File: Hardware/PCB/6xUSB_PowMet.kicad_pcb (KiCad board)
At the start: 2 copper layers, 73.2 x 66.8 mm, 109 parts, among them CON1 BARREL_JACK, IC1 ATMEGA32-M, P1 USB_A, P10 USB_B, P2 USB_A, P3 USB_A, P4 USB_A, P5 USB_A, P6 USB_A, P7 CONN_01X08, P8 CONN_01X03, Q1 IRFR5305PBF, U1 LM1117MP-2.5, U10 TPS5450-EP_DDA_8, U11 LTC4412, U2 LT6106, U3 LT6106, U4 LT6106, U5 LT6106, U6 LT6106, U7 LT6106, U8 AP1117E33, U9 FE1.1s, Y1 12Mhz

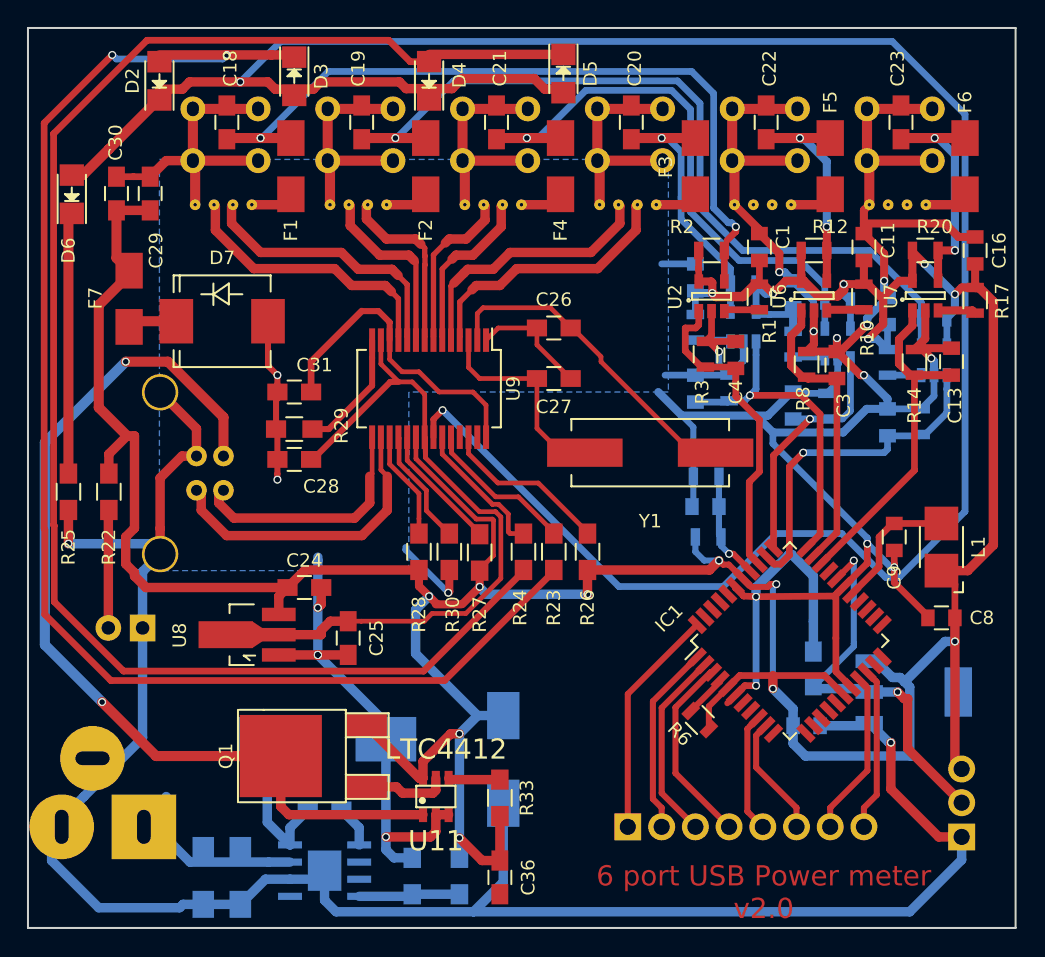
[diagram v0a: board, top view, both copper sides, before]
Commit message: Updated pcb
Updated schematic and solved some pcb mistakes
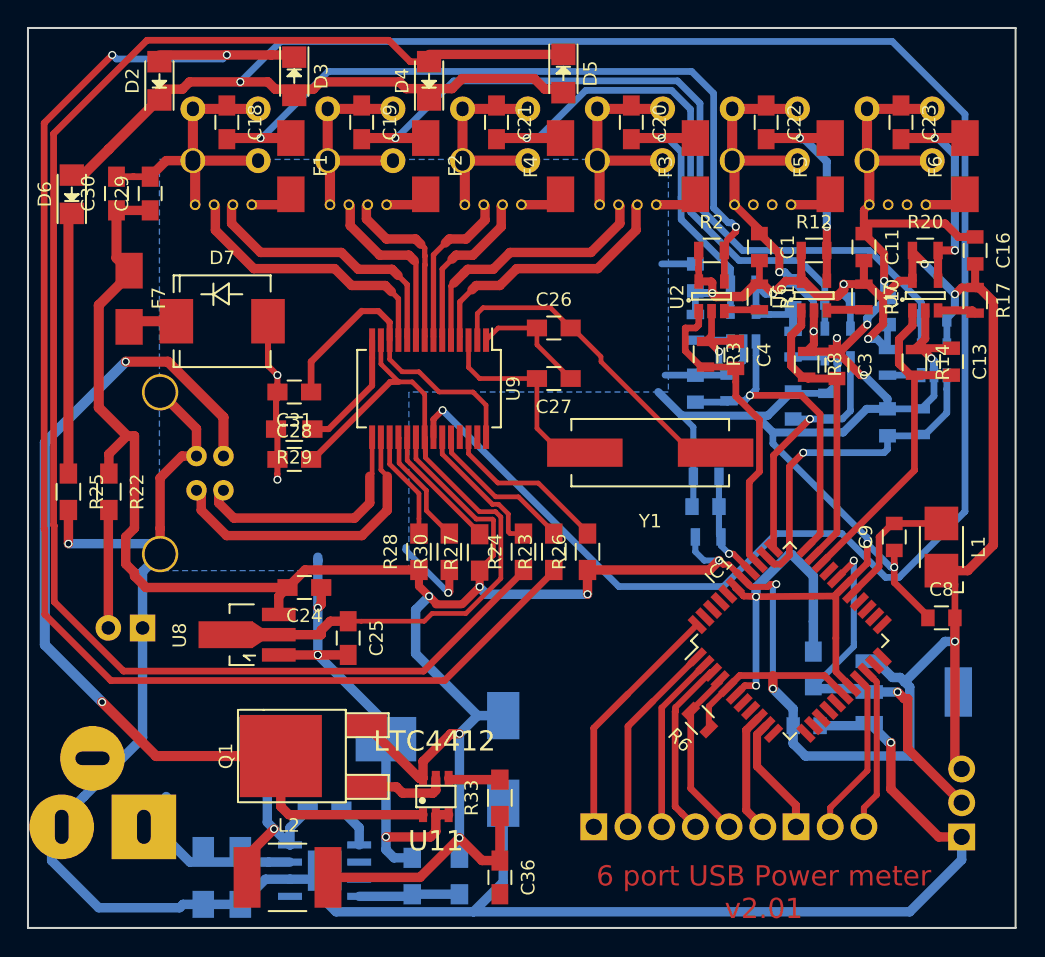
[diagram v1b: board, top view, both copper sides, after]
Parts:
- added L2: 10uH, Inductors_NEOSID:Neosid_Inductor_SM-NE56_SMD2220, F.Cu at (114.5, 111.5)
- added P9: CONN_01X03, Connect:Wafer_Vertical10x5.8x7RM2.5-3, B.Cu at (152.2, 107.8)
- P7: value CONN_01X08 -> CONN_01X06; footprint Connect:Wafer_Vertical22.5x5.8x7RM2.5-8 -> Connect:Wafer_Vertical17.5x5.8x7RM2.5-6
- moved P7 2.52 mm to (137.2, 107.8)
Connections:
- IC1 pad 4: Net-(IC1-Pad4) -> RST
- P7 pad 5: RXD -> RST
- P7 pad 6: TXD -> RXD
- R6 pad 2: Net-(IC1-Pad4) -> RST
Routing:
- net RST: track 0.00 -> 13.0 mm
- net +5V: track 305.5 -> 316.4 mm
- net Net-(C34-Pad1): track 11.7 -> 16.1 mm, vias 0 -> 1
- net Net-(IC1-Pad4): track 3.21 -> 0.00 mm
- net SS: track 17.1 -> 18.2 mm
- net MISO: track 14.4 -> 13.4 mm
- net SCK: track 14.3 -> 13.3 mm
- net GND: track 495.7 -> 494.9 mm
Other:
- board text added: "6 port USB Power meter v2.01"
- board text removed: "6 port USB Power meter v2.0"

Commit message: Upd_sch
Updated schematic and PCB
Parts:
- D7: footprint Diodes_SMD:SMC_Standard -> Diodes_SMD:SOD-123
- Y1: footprint Crystals:Crystal_HC49-SD_SMD -> Crystals:Crystal_SMD_5032_4Pads
- moved Y1 2.95 mm to (138.8, 78.7)
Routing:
- net GND: track 494.9 -> 506.6 mm, vias 21 -> 22
- net Net-(C26-Pad2): track 24.5 -> 18.7 mm
- net Net-(D7-Pad1): track 3.67 -> 5.44 mm

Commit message: Upd
Schematic updates and PCB
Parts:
- removed C32, C33: 47uF, Capacitors_SMD:C_1206_HandSoldering
- removed C34: 10n, Capacitors_SMD:C_0805_HandSoldering
- removed C35: 180uF, Capacitors_SMD:c_elec_8x10.5
- removed CON1: BARREL_JACK, Connect:JACK_ALIM
- removed L2: 10uH, Inductors_NEOSID:Neosid_Inductor_SM-NE56_SMD2220
- removed U10: TPS5450-EP_DDA_8, TPS5450-EP_DDA_8:DDA8_3X2P49
- added C37: 22uF, Capacitors_SMD:C_1206, F.Cu at (108.0, 100.2)
- added C38: 100nF, Capacitors_SMD:C_0805, F.Cu at (110.9, 103.8)
- added C39: 15nF, Capacitors_SMD:C_0805, F.Cu at (114.8, 102.5)
- added C40: 470nF, Capacitors_SMD:C_0805, F.Cu at (130.9, 101.6)
- added C41: 1uF, Capacitors_SMD:C_0805, F.Cu at (110.8, 99.8)
- added C42: 470pF, Capacitors_SMD:C_0805, F.Cu at (121.6, 112.4)
- added C43: 220uF, Capacitors_SMD:c_elec_6.3x5.3, F.Cu at (129.0, 111.2)
- added CON2: BARREL_JACK, Connect:JACK_ALIM, B.Cu at (100.8, 108.7)
- added D10: SKL14, Diodes_SMD:SOD-123, F.Cu at (108.9, 69.4)
- added D11: SK2030YD2, Diodes_SMD:DD-PAK_TO263_DualDiode, B.Cu at (139.0, 99.6)
- added D12: Power, LEDs:LED-5MM, B.Cu at (163.2, 82.0)
- added D9: Power, LEDs:LED-5MM, B.Cu at (100.2, 99.4)
- added L3: 2.2uH, Inductors:SELF-WE-PD-XXL, B.Cu at (122.8, 105.8)
- added Q2: CSD16342Q5A, Personal:AB2_SON5x6_FET, F.Cu at (114.8, 110.2)
- added Q3: CSD17577Q5A, Personal:AB2_SON5x6_FET, F.Cu at (132.4, 97.7)
- added R34: 100K, Resistors_SMD:R_0805, F.Cu at (114.1, 105.8)
- added R35: 1K07, Resistors_SMD:R_0805, F.Cu at (128.8, 104.2)
- added R36: 73K2, Capacitors_SMD:C_0805, F.Cu at (121.6, 109.4)
- added R37: 10K, Capacitors_SMD:C_0805, F.Cu at (121.6, 106.5)
- added R38: 330, Resistors_SMD:R_0805_HandSoldering, F.Cu at (104.2, 96.8)
- added U13: LM3150, Housings_SSOP:SSOP-14_5.3x6.2mm_Pitch0.65mm, F.Cu at (121.7, 101.4)
- C24: value 4.7uF -> 10uF; moved to B.Cu
- C25: value 4.7uF -> 22uF; moved to B.Cu
- C28, C36, Q1, R33, U11: moved to B.Cu
- C6: footprint Capacitors_SMD:C_0805_HandSoldering -> Capacitors_SMD:C_0805
- D2, D3, D4, D5, D6: footprint LEDs:LED_1206 -> LEDs:LED_0805
- D7: footprint Diodes_SMD:SOD-123 -> Diodes_SMD:MiniMELF_Standard
- D8: value D_Schottky -> Power; footprint Diodes_SMD:SMC_Handsoldering -> LEDs:LED-5MM
- F7: value F_Small -> 500mA
- R31: value 10K -> 330
- R32: value 3.24K -> 330
- R5: value 14K -> 15K
- U8: footprint TO_SOT_Packages_SMD:SOT89-3_Housing_Handsoldering -> TO_SOT_Packages_SMD:SOT-223; moved to B.Cu
- U9: footprint Housings_SSOP:SSOP-28_5.3x10.2mm_Pitch0.65mm -> Housings_SSOP:TSSOP-28_4.4x9.7mm_Pitch0.65mm
- moved R32 46.9 mm to (163.9, 87.2), turned to 90 degrees
- moved D8 46.7 mm to (159.9, 82.0), turned to 180 degrees
- moved R31 41.8 mm to (161.4, 87.2)
- moved U8 26.9 mm to (137.8, 88.2), turned to 0 degrees
- moved C24 26.2 mm to (140.2, 80.7), turned to 270 degrees
- moved R25 24.1 mm to (99.0, 58.9)
- moved C25 23.0 mm to (137.8, 80.5), turned to 90 degrees
- moved D1 23.0 mm to (100.2, 70.3), turned to 90 degrees
- moved C36 21.1 mm to (130.0, 90.5), turned to 0 degrees
- moved R22 17.5 mm to (108.2, 66.8), turned to 180 degrees
- moved R33 16.0 mm to (122.5, 91.5), turned to 270 degrees
- moved U11 12.1 mm to (125.7, 93.4), turned to 180 degrees
- moved C28 9.75 mm to (124.6, 82.2), turned to 90 degrees
- moved R26 8.91 mm to (131.7, 80.0), turned to 180 degrees
- moved Q1 8.85 mm to (119.0, 93.8), turned to 270 degrees
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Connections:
- net /USB hub/3V3 renamed +3.3V
- D7 pad 1: Net-(D7-Pad1) -> +5V
- D8 pad 1: Net-(C34-Pad1) -> GND
- D8 pad 2: GND -> Net-(D8-Pad2)
- F7 pad 1: +5V -> USB_P
- F7 pad 2: Net-(D7-Pad1) -> Net-(F7-Pad2)
- IC1 pad 25: Net-(IC1-Pad25) -> PC6_25
- IC1 pad 26: Net-(IC1-Pad26) -> PC7_26
- P10 pad 1: VREG -> Net-(F7-Pad2)
- Q1 pad 2: VREG -> +5V
- R22 pad 1: +5V -> USB_P
- R31 pad 1: Net-(R31-Pad1) -> PC7_26
- R31 pad 2: +5V -> Net-(D8-Pad2)
- R32 pad 1: GND -> PC6_25
- R32 pad 2: Net-(R31-Pad1) -> Net-(D12-Pad2)
- U11 pad 1: VREG -> +5V
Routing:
- net VREG: track 70.8 -> 0.00 mm, vias 2 -> 0
- net Net-(D2-Pad1): track 178.5 -> 110.1 mm
- net Net-(C42-Pad1): track 0.00 -> 59.2 mm, vias 0 -> 2
- net GND: track 506.6 -> 449.7 mm, vias 22 -> 23
- net Net-(C40-Pad1): track 0.00 -> 32.3 mm, vias 0 -> 2
- net Net-(C37-Pad1): track 0.00 -> 29.5 mm
- net Net-(C42-Pad2): track 0.00 -> 23.8 mm, vias 0 -> 2
- net +3.3V: track 53.0 -> 31.7 mm, vias 0 -> 2
- net +5V: track 316.4 -> 336.8 mm
- net Net-(D6-Pad1): track 19.4 -> 2.56 mm
- net Net-(C34-Pad1): track 16.1 -> 0.00 mm, vias 1 -> 0
- net Net-(Q2-Pad4): track 0.00 -> 15.1 mm, vias 0 -> 2
- net Net-(C32-Pad1): track 13.0 -> 0.00 mm
- net Net-(F7-Pad2): track 0.00 -> 9.16 mm
- net Net-(R26-Pad2): track 12.6 -> 4.32 mm
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- added copper zone on F.Cu, net GND
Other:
- board text added: "6 port USB Power meter v2.1"
- board text removed: "6 port USB Power meter v2.01"

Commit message: updates
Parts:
- removed D12, D8: Power, LEDs:LED-5MM
- removed D4, D5: Led_Small, LEDs:LED_0805
- removed D7: 5.1V, Diodes_SMD:MiniMELF_Standard
- removed IC1: ATMEGA32-M, Housings_QFP:TQFP-44_10x10mm_Pitch0.8mm
- removed P7: CONN_01X06, Connect:Wafer_Vertical17.5x5.8x7RM2.5-6
- removed P8, P9: CONN_01X03, Connect:Wafer_Vertical10x5.8x7RM2.5-3
- added C32: 22pF, Capacitors_SMD:C_0603, F.Cu at (146.7, 101.3)
- added C33: 0.1uF, Capacitors_SMD:C_0603, F.Cu at (149.4, 106.2)
- added C34: 100n, Capacitors_SMD:C_0805, B.Cu at (175.1, 104.0)
- added C35: 100n, Capacitors_SMD:C_0805, B.Cu at (179.5, 95.3)
- added C44: 10uF, Capacitors_SMD:C_0805, F.Cu at (185.1, 86.6)
- added C45: 10uF, Capacitors_SMD:C_0805, B.Cu at (181.9, 95.3)
- added C46: 22uF, Capacitors_Tantalum_SMD:CP_Tantalum_Case-R_EIA-2012-12_Reflow, F.Cu at (182.4, 127.0)
- added C47: 1uF, Capacitors_SMD:C_0805, F.Cu at (108.5, 124.3)
- added C48: 100n, Capacitors_SMD:C_0805, F.Cu at (202.2, 76.2)
- added C49: 1uF, Capacitors_SMD:C_0805, F.Cu at (135.6, 131.4)
- added C51: 47uF, Capacitors_SMD:C_1206, F.Cu at (200.9, 119.2)
- added C52: 18pF, Capacitors_SMD:C_0805, F.Cu at (121.8, 37.3)
- added F8: MSMF050-2, Resistors_SMD:R_1812, F.Cu at (185.8, 138.5)
- added J1: MICROUSB, kicad-libs-master:USB-MICRO-B-FCI-10118193, F.Cu at (87.2, 128.3)
- added J2: CONN_01X04, Connectors_JST:JST_EH_B04B-EH-A_04x2.50mm_Straight, F.Cu at (105.8, 140.7)
- added J3: CONN_01X11, Connectors_JST:JST_EH_B11B-EH-A_11x2.50mm_Straight, F.Cu at (139.8, 124.4)
- added L10: WE-CNSW, Inductors_SMD:L_CommonMode_Wuerth_WE-CNSW, F.Cu at (76.2, 102.5)
- added L11: WE-CBF, Inductors_SMD:L_0603, F.Cu at (120.3, 61.6)
- added L12: WE-CBF, Inductors_SMD:L_0603, F.Cu at (170.4, 45.5)
- added L2: WE-CNSW, Inductors_SMD:L_CommonMode_Wuerth_WE-CNSW, F.Cu at (135.2, 64.4)
- added L4: Bead/100MHZ/470ohm/2A, Resistors_SMD:R_0805_HandSoldering, B.Cu at (97.4, 66.0)
- added L5: WE-CNSW, Inductors_SMD:L_CommonMode_Wuerth_WE-CNSW, F.Cu at (125.7, 64.4)
- added L6: WE-CNSW, Inductors_SMD:L_CommonMode_Wuerth_WE-CNSW, F.Cu at (118.5, 64.4)
- added L7: WE-CNSW, Inductors_SMD:L_CommonMode_Wuerth_WE-CNSW, F.Cu at (109.2, 64.4)
- added L8: WE-CBF, Inductors_SMD:L_0603, F.Cu at (107.8, 61.6)
- added L9: WE-CBF, Inductors_SMD:L_0603, F.Cu at (132.8, 61.6)
- added LED1: Led_Small, Inductors_SMD:L_1806, F.Cu at (102.6, 49.7)
- added LED2: Led_Small, Inductors_SMD:L_1806, F.Cu at (115.2, 49.8)
- added LED3: Led_Small, Inductors_SMD:L_1806, F.Cu at (127.6, 49.8)
- added LED4: Led_Small, Inductors_SMD:L_1806, F.Cu at (140.1, 49.8)
- added P11: CONN_02X04, Socket_Strips:Socket_Strip_Straight_2x04, B.Cu at (162.6, 69.3)
- added P12: CONN_02X04, Socket_Strips:Socket_Strip_Straight_2x04, B.Cu at (174.4, 69.2)
- added P13: Burn, Pin_Headers:Pin_Header_Straight_2x01, B.Cu at (185.1, 78.9)
- added Q10: IRLML6401, TO_SOT_Packages_SMD:SOT-23, F.Cu at (200.4, 104.8)
- added Q5: IRLML6401, TO_SOT_Packages_SMD:SOT-23, B.Cu at (142.6, 69.8)
- added Q6: IRLML6401, TO_SOT_Packages_SMD:SOT-23, B.Cu at (158.3, 53.1)
- added Q7: IRLML6401, TO_SOT_Packages_SMD:SOT-23, F.Cu at (157.6, 65.1)
- added Q8: IRLML6401, TO_SOT_Packages_SMD:SOT-23, B.Cu at (176.6, 77.2)
- added Q9: IRLML6401, TO_SOT_Packages_SMD:SOT-23, F.Cu at (148.1, 61.8)
- added R39: 10K, Resistors_SMD:R_0805, B.Cu at (180.1, 104.0)
- added R40: 10K, Resistors_SMD:R_0805, F.Cu at (141.4, 90.8)
- added R41: 100R, Resistors_SMD:R_0805, B.Cu at (180.1, 100.1)
- added R42: 10K, Resistors_SMD:R_0805, F.Cu at (140.9, 86.8)
- added R43: 100R, Resistors_SMD:R_0805, B.Cu at (157.2, 93.2)
- added R44: 100R, Resistors_SMD:R_0805, F.Cu at (123.4, 82.8)
- added R45: 100K, Resistors_SMD:R_0805, F.Cu at (115.1, 73.0)
- added R46: 470R, Resistors_SMD:R_0805, B.Cu at (177.2, 104.0)
- added R47: 100R, Resistors_SMD:R_0805, B.Cu at (174.2, 90.8)
- added R48: 150R, Resistors_SMD:R_0805, B.Cu at (174.2, 98.0)
- added R49: 150R, Resistors_SMD:R_0805, B.Cu at (174.2, 94.3)
- added RV1: CG0603MLC-05E, Inductors_SMD:L_0603, F.Cu at (204.4, 85.4)
- added RV2: CG0603MLC-05E, Inductors_SMD:L_0603, F.Cu at (87.0, 121.2)
- added SW1: Reset, Buttons_Switches_SMD:SW_SPST_B3U-1000P, F.Cu at (179.8, 84.1)
- added SW2: Reset, Buttons_Switches_SMD:SW_SPST_B3U-3000P, F.Cu at (197.8, 130.6)
- added TP1: TEST, Measurement_Points:Measurement_Point_Round-SMD-Pad_Small, B.Cu at (169.3, 97.8)
- added U10: ESP-07v2, ESP8266:ESP-12E, F.Cu at (185.6, 105.0)
- added U12: 5v to 3.3v LDO, TO_SOT_Packages_SMD:SOT-223-3Lead_TabPin2, B.Cu at (180.2, 83.7)
- added U14: LT6106, TO_SOT_Packages_SMD:SOT-23-5, F.Cu at (147.2, 144.1)
- added Y2: 16.000 Mhz, Crystals:Crystal_SMD_5032-4pin_5.0x3.2mm, F.Cu at (147.4, 104.2)
- C1, C16, D10, R3, R8, U2, U6, U7: moved to B.Cu
- C11: value 100n -> 1nF; moved to B.Cu
- C12, C14: value 1n -> 1nF; moved to F.Cu
- C13: value 1n -> 1nF; moved to B.Cu
- C15, C17, R13, R15, U5: moved to F.Cu
- C18, C19, C20, C29: footprint Capacitors_SMD:C_0805_HandSoldering -> Capacitors_SMD:C_0805
- C2: value 1n -> 0.33uF
- C21, C22, C23: value 10uF -> 1nF; footprint Capacitors_SMD:C_0805_HandSoldering -> Capacitors_SMD:C_0805
- C24, C30: value 10uF -> 0.1uF; footprint Capacitors_SMD:C_0805_HandSoldering -> Capacitors_SMD:C_0603
- C25: value 22uF -> 22pF; footprint Capacitors_SMD:C_0805_HandSoldering -> Capacitors_SMD:C_0603
- C26: value 10pF -> 18pF; footprint Capacitors_SMD:C_0805_HandSoldering -> Capacitors_SMD:C_0805
- C27: value 10pF -> 100n; footprint Capacitors_SMD:C_0805_HandSoldering -> Capacitors_SMD:C_0805
- C28: footprint Capacitors_SMD:C_0805_HandSoldering -> Capacitors_SMD:C_0805; moved to F.Cu
- C3, C4: value 1n -> 100n; moved to B.Cu
- C31: value 10uF -> 47uF; footprint Capacitors_SMD:C_0805_HandSoldering -> Capacitors_SMD:C_1206; moved to B.Cu
- C36: value 100nF -> 10uF; footprint Capacitors_SMD:C_0805_HandSoldering -> Capacitors_SMD:C_0805
- C37: value 22uF -> 47uF
- C38: value 100nF -> 100n
- C42: value 470pF -> 1nF
- C43: value 220uF -> 330uF; footprint Capacitors_SMD:c_elec_6.3x5.3 -> Capacitors_SMD:CP_Elec_6.3x5.8; moved to B.Cu
- C6: value 10uF -> 100n
- C7: value 1n -> 100n
- D1: value Power -> USB Power; footprint LEDs:LED-5MM -> LEDs:LED_D3.0mm_Horizontal_O6.35mm_Z6.0mm
- D11: value SK2030YD2 -> SK152-TP; footprint Diodes_SMD:DD-PAK_TO263_DualDiode -> agg:DO-214AB-SMC
- D2: value Led_Small -> MC Status; footprint LEDs:LED_0805 -> LEDs:LED_0603
- D3: value Led_Small -> CD1206-S01575; footprint LEDs:LED_0805 -> Diodes_SMD:D_1206
- D6: value Led_Small -> Led_Small_3mm; footprint LEDs:LED_0805 -> LEDs:LED_D3.0mm_Horizontal_O6.35mm_Z6.0mm
- D9: value Power -> Power DC; footprint LEDs:LED-5MM -> LEDs:LED_D3.0mm_Horizontal_O6.35mm_Z6.0mm
- F1, F2, F3, F4, F5, F6: footprint Fuse_Holders_and_Fuses:Fuse_SMD1206_HandSoldering -> Fuse_Holders_and_Fuses:Fuse_SMD1206_Reflow
- F7: value 500mA -> MSMF050-2; footprint Fuse_Holders_and_Fuses:Fuse_SMD1206_HandSoldering -> Resistors_SMD:R_1812
- L1: value 10uH -> MH2029-300Y; footprint Inductors:Inductor_1212 -> Inductors_SMD:L_0805
- L3: value 2.2uH -> 4.7uH 5.2mOhm
- P1, P2, P3, P4, P5, P6: footprint USB-A_vertical1:USB_A_Vertical -> USB_A_Vertical:USB_A_Vertical
- Q2: value CSD16342Q5A -> CSD16321Q5
- Q3: value CSD17577Q5A -> CSD18509Q5B
- R1: value 100R -> 470R; moved to B.Cu
- R10, R17: value 100R -> 10K; moved to B.Cu
- R11: value 0.01R -> 0.02R; footprint Resistors_SMD:R_0805 -> Resistors_SMD:R_1206
- R12, R2, R20: value 0.01R -> 0.02R; footprint Resistors_SMD:R_0805 -> Resistors_SMD:R_1206; moved to B.Cu
- R14: value 10K -> 100R; moved to B.Cu
- R16, R19: value 100R -> 10K; moved to F.Cu
- R18, R21: value 0.01R -> 0.02R; footprint Resistors_SMD:R_0805 -> Resistors_SMD:R_1206; moved to F.Cu
- R22, R23, R24, R25: value 330 -> 100R; footprint Resistors_SMD:R_0805_HandSoldering -> Resistors_SMD:R_0805
- R26, R27, R29, R30, R31, R33: footprint Resistors_SMD:R_0805_HandSoldering -> Resistors_SMD:R_0805
- R28: value 10K -> 100K; footprint Resistors_SMD:R_0805_HandSoldering -> Resistors_SMD:R_0805
- R32: value 330 -> 22R; footprint Resistors_SMD:R_0805_HandSoldering -> Resistors_SMD:R_0805
- R34: value 100K -> 237K
- R36, R37: footprint Capacitors_SMD:C_0805 -> Resistors_SMD:R_0805
- R38: value 330 -> 100K; footprint Resistors_SMD:R_0805_HandSoldering -> Resistors_SMD:R_0805
- R6: value 10k -> 10K
- R7: value 10K -> 22R
- R9: value 100R -> 10K
- U1: value LM1117MP-2.5 -> 24LC02; footprint TO_SOT_Packages_SMD:SOT-223 -> Housings_SOIC:SOIC-8_3.9x4.9mm_Pitch1.27mm
- U11: footprint tom_kicad_lib:SOT-6 -> TO_SOT_Packages_SMD:SOT-23-6
- U3: value LT6106 -> ATMEGA32U4-AU; footprint TO_SOT_Packages_SMD:SOT-23-5 -> Housings_QFP:LQFP-44_10x10mm_Pitch0.8mm; moved to F.Cu
- U8: value AP1117E33 -> LM4040N-4.1; footprint TO_SOT_Packages_SMD:SOT-223 -> TO_SOT_Packages_SMD:SOT-23
- Y1: footprint Crystals:Crystal_SMD_5032_4Pads -> Crystals:Crystal_HC49-SD_SMD
- moved D3 102.0 mm to (206.1, 98.0), turned to 0 degrees
- moved D2 51.5 mm to (142.9, 86.6), turned to 270 degrees
- moved P6 36.4 mm to (176.2, 54.7)
- moved U1 36.4 mm to (129.4, 79.7), turned to 270 degrees
- moved C30 29.5 mm to (121.5, 82.8)
- moved C29 28.5 mm to (129.2, 74.8)
- moved C31 26.5 mm to (108.0, 101.0), turned to 90 degrees
- moved U3 23.7 mm to (151.5, 94.2), turned to 45 degrees
- moved P5 20.0 mm to (139.8, 54.5)
- moved R30 18.1 mm to (144.8, 87.7)
- moved U8 17.0 mm to (154.1, 93.2), turned to 270 degrees
- moved C24 17.0 mm to (124.8, 73.7)
- moved R20 16.6 mm to (172.9, 77.3), turned to 90 degrees
- moved F6 16.4 mm to (181.1, 58.9)
- moved C23 16.3 mm to (176.3, 55.7)
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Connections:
- C1 pad 2: +5V -> Net-(C1-Pad2)
- C10 pad 1: GND -> +4.096V
- C10 pad 2: +5V -> GND
- C11 pad 2: +5V -> Net-(C11-Pad2)
- C2 pad 1: GND -> +5V
- C2 pad 2: Net-(C2-Pad2) -> GND
- C25 pad 1: +3.3V -> Net-(C25-Pad1)
- C26 pad 1: Net-(C26-Pad1) -> GND
- C27 pad 1: Net-(C26-Pad1) -> GND
- C27 pad 2: Net-(C27-Pad2) -> +5V
- C28 pad 2: +3.3V -> /USB hub/3V3
- C29 pad 1: +5V -> Net-(C29-Pad1)
- C3 pad 2: Net-(C3-Pad2) -> +5V
- C30 pad 1: +5V -> Net-(C30-Pad1)
- C30 pad 2: GND -> Net-(C30-Pad2)
- C31 pad 1: /USB hub/1V8 -> Net-(C31-Pad1)
- C36 pad 1: +5V -> GND
- C36 pad 2: GND -> Net-(C36-Pad2)
- C37 pad 1: Net-(C37-Pad1) -> Net-(C31-Pad1)
- C38 pad 1: Net-(C37-Pad1) -> Net-(C31-Pad1)
- C4 pad 2: Net-(C4-Pad2) -> +5V
- C43 pad 2: Net-(C42-Pad2) -> GND
- C5 pad 1: +5V -> +3v3
- C6 pad 1: +2.5V -> +3v3
- C7 pad 1: GND -> VBUS
- C7 pad 2: Net-(C7-Pad2) -> GND
- C8 pad 1: GND -> +5V
- C8 pad 2: +5V -> GND
- C9 pad 1: GND -> +4.096V
- C9 pad 2: Net-(C9-Pad2) -> GND
- CON2 pad 1: Net-(C37-Pad1) -> Net-(C31-Pad1)
- D10 pad 1: +5V -> VREG
- D10 pad 2: USB_P -> Net-(D10-Pad2)
- D2 pad 1: Net-(D2-Pad1) -> GND
- D3 pad 1: Net-(D2-Pad2) -> +5V
- D3 pad 2: Net-(D2-Pad1) -> RST
- D6 pad 2: Net-(D2-Pad1) -> Net-(D6-Pad2)
- F1 pad 1: Net-(C18-Pad2) -> Net-(F1-Pad1)
- F1 pad 2: Net-(F1-Pad2) -> Net-(C18-Pad2)
- F2 pad 1: Net-(C19-Pad2) -> Net-(F2-Pad1)
- F2 pad 2: Net-(F2-Pad2) -> Net-(C36-Pad2)
- F4 pad 2: Net-(C21-Pad2) -> Net-(C19-Pad2)
- F5 pad 2: Net-(C22-Pad2) -> Net-(C44-Pad2)
- F6 pad 2: Net-(C23-Pad2) -> Net-(C45-Pad2)
- L1 pad 2: Net-(C9-Pad2) -> Net-(C47-Pad2)
- P1 pad 1: Net-(F1-Pad2) -> Net-(L8-Pad1)
- P2 pad 1: Net-(F4-Pad1) -> Net-(L9-Pad1)
- P3 pad 1: Net-(F5-Pad1) -> Net-(P11-Pad8)
- P3 pad 4: GND -> Net-(P11-Pad2)
- P3 pad 5: GND -> Net-(P11-Pad2)
- P4 pad 1: Net-(F2-Pad2) -> Net-(L11-Pad1)
- P5 pad 1: Net-(F6-Pad1) -> Net-(L12-Pad1)
- P5 pad 2: Net-(P5-Pad2) -> D4-
- P5 pad 3: Net-(P5-Pad3) -> D4+
- P6 pad 1: Net-(F3-Pad1) -> Net-(P12-Pad8)
- P6 pad 2: D4- -> Net-(P12-Pad6)
- P6 pad 3: D4+ -> Net-(P12-Pad4)
- P6 pad 4: GND -> Net-(P12-Pad2)
- P6 pad 5: GND -> Net-(P12-Pad2)
- Q1 pad 2: +5V -> VREG
- Q2 pad 5: Net-(C37-Pad1) -> Net-(C31-Pad1)
- Q2 pad 6: Net-(C37-Pad1) -> Net-(C31-Pad1)
- Q2 pad 7: Net-(C37-Pad1) -> Net-(C31-Pad1)
- Q2 pad 8: Net-(C37-Pad1) -> Net-(C31-Pad1)
- R1 pad 1: +5V -> Net-(C1-Pad2)
- R10 pad 1: +5V -> Net-(P13-Pad1)
- R10 pad 2: Net-(R10-Pad2) -> +3v3
- R11 pad 2: Net-(C21-Pad2) -> Net-(Q5-Pad2)
- R12 pad 2: Net-(C22-Pad2) -> Net-(Q6-Pad2)
- R13 pad 1: GND -> Net-(R13-Pad1)
- R13 pad 2: Net-(C12-Pad2) -> +3v3
- R14 pad 1: GND -> +5V
- R14 pad 2: Net-(C13-Pad2) -> +4.096V
- R15 pad 1: GND -> Net-(C11-Pad2)
- R15 pad 2: Net-(C14-Pad2) -> GND
- R16 pad 1: +5V -> Net-(C12-Pad2)
- R16 pad 2: Net-(R16-Pad2) -> GND
- R17 pad 1: +5V -> Net-(C13-Pad2)
- R17 pad 2: Net-(R17-Pad2) -> GND
- R18 pad 2: Net-(C19-Pad2) -> Net-(Q7-Pad2)
- R19 pad 1: +5V -> Net-(C14-Pad2)
- R19 pad 2: Net-(R19-Pad2) -> GND
- R2 pad 2: Net-(C18-Pad2) -> Net-(Q10-Pad2)
- R20 pad 2: Net-(C23-Pad2) -> Net-(Q8-Pad2)
- R21 pad 2: Net-(C20-Pad2) -> Net-(Q9-Pad2)
- R22 pad 1: USB_P -> +5V
- R22 pad 2: Net-(D1-Pad2) -> Net-(R22-Pad2)
- R23 pad 1: Net-(D2-Pad2) -> Net-(LED1-Pad1)
- R24 pad 1: Net-(D4-Pad2) -> +5V
- R25 pad 1: Net-(D6-Pad1) -> +5V
- R25 pad 2: GND -> Net-(R25-Pad2)
- R26 pad 1: +5V -> PB0_40
- R26 pad 2: Net-(R26-Pad2) -> GND
- R27 pad 1: +5V -> VREG
- R27 pad 2: Net-(R27-Pad2) -> Net-(C30-Pad2)
- R28 pad 1: +5V -> Net-(C30-Pad1)
- R28 pad 2: Net-(R28-Pad2) -> Net-(C30-Pad2)
- R3 pad 1: GND -> Net-(R3-Pad1)
- R3 pad 2: Net-(C4-Pad2) -> +3v3
- R30 pad 1: GND -> Net-(C21-Pad2)
- R30 pad 2: Net-(R30-Pad2) -> GND
- R31 pad 1: PC7_26 -> Net-(C42-Pad1)
- R31 pad 2: Net-(D8-Pad2) -> Net-(D9-Pad2)
- R32 pad 1: PC6_25 -> D-
- R33 pad 2: Net-(R33-Pad2) -> PB0_40
- R34 pad 2: Net-(C37-Pad1) -> Net-(C31-Pad1)
- R38 pad 1: Net-(C42-Pad1) -> /USB hub/3V3
- R38 pad 2: Net-(D9-Pad2) -> Net-(R38-Pad2)
- R4 pad 1: GND -> +5V
- R4 pad 2: Net-(C7-Pad2) -> RST
- R5 pad 2: Net-(C7-Pad2) -> Net-(C11-Pad2)
- R6 pad 1: +5V -> Net-(C1-Pad2)
- R6 pad 2: RST -> +3v3
- R7 pad 1: GND -> D+
- R7 pad 2: Net-(C2-Pad2) -> Net-(J1-Pad3)
- R8 pad 2: Net-(C3-Pad2) -> VBUS
- R9 pad 1: +5V -> GND
- U1 pad 2: +2.5V -> GND
- U1 pad 3: +5V -> GND
- U1 pad 4: Net-(U1-Pad4) -> GND
- U11 pad 1: +5V -> VREG
- U11 pad 4: Net-(R33-Pad2) -> PB0_40
- U13 pad 2: Net-(C37-Pad1) -> Net-(C31-Pad1)
- U2 pad 1: Net-(C4-Pad2) -> Net-(C12-Pad2)
- U2 pad 3: Net-(R1-Pad2) -> Net-(R22-Pad2)
- U2 pad 4: Net-(C18-Pad2) -> Net-(Q10-Pad2)
- U3 pad 1: Net-(C12-Pad2) -> USB_1
- U3 pad 2: GND -> +5V
- U3 pad 3: Net-(R16-Pad2) -> D-
- U3 pad 4: Net-(C19-Pad2) -> D+
- U3 pad 5: +5V -> GND
- U4 pad 1: Net-(C2-Pad2) -> Net-(C13-Pad2)
- U4 pad 3: Net-(R9-Pad2) -> Net-(R24-Pad2)
- U4 pad 4: Net-(C21-Pad2) -> Net-(Q5-Pad2)
- U5 pad 3: Net-(R19-Pad2) -> Net-(R25-Pad2)
- U5 pad 4: Net-(C20-Pad2) -> Net-(Q6-Pad2)
- U6 pad 1: Net-(C3-Pad2) -> Net-(C21-Pad2)
- U6 pad 3: Net-(R10-Pad2) -> Net-(R41-Pad2)
- U6 pad 4: Net-(C22-Pad2) -> Net-(Q7-Pad2)
- U7 pad 1: Net-(C13-Pad2) -> Net-(C22-Pad2)
- U7 pad 3: Net-(R17-Pad2) -> Net-(R43-Pad2)
- U7 pad 4: Net-(C23-Pad2) -> Net-(Q8-Pad2)
- U8 pad 1: GND -> +4.096V
- U8 pad 2: +3.3V -> GND
- U8 pad 3: +5V -> (no net)
- U9 pad 1: Net-(C26-Pad1) -> GND
- U9 pad 10: D1- -> Net-(L7-Pad4)
- U9 pad 11: D1+ -> Net-(L7-Pad1)
- U9 pad 12: /USB hub/1V8 -> Net-(U9-Pad12)
- U9 pad 13: +3.3V -> Net-(U9-Pad13)
- U9 pad 15: D5- -> Net-(L10-Pad3)
- U9 pad 16: D5+ -> Net-(L10-Pad2)
- U9 pad 17: Net-(R28-Pad2) -> Net-(R38-Pad2)
- U9 pad 18: Net-(R30-Pad2) -> Net-(C30-Pad2)
- U9 pad 19: Net-(R27-Pad2) -> Net-(R45-Pad2)
- U9 pad 21: +3.3V -> /USB hub/3V3
- U9 pad 22: Net-(D2-Pad1) -> Net-(D6-Pad2)
- U9 pad 23: Net-(R24-Pad2) -> /USB hub/LED1
- U9 pad 26: Net-(R26-Pad2) -> Net-(C29-Pad1)
- U9 pad 27: Net-(U9-Pad27) -> /USB hub/TESTJ
- U9 pad 28: /USB hub/1V8 -> Net-(U9-Pad28)
- U9 pad 3: Net-(C27-Pad2) -> Net-(C52-Pad2)
- U9 pad 4: D4- -> Net-(L2-Pad4)
- U9 pad 5: D4+ -> Net-(L2-Pad1)
- U9 pad 6: D3- -> Net-(L5-Pad4)
- U9 pad 7: D3+ -> Net-(L5-Pad1)
- U9 pad 8: D2- -> Net-(L6-Pad4)
- U9 pad 9: D2+ -> Net-(L6-Pad1)
- Y1 pad 2: Net-(C27-Pad2) -> Net-(C52-Pad2)
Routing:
- net GND: track 449.7 -> 214.1 mm
- net Net-(LED1-Pad1): track 0.00 -> 133.1 mm, vias 0 -> 3
- net Net-(D4-Pad2): track 111.4 -> 0.00 mm
- net Net-(D2-Pad1): track 110.1 -> 0.00 mm, vias 2 -> 0
- net Net-(D2-Pad2): track 106.1 -> 0.95 mm, vias 2 -> 0
- net Net-(D6-Pad2): track 0.00 -> 98.1 mm, vias 0 -> 2
- net +5V: track 336.8 -> 264.2 mm, vias 15 -> 21
- net Net-(C31-Pad1): track 0.00 -> 72.3 mm, vias 0 -> 4
- net Net-(C42-Pad1): track 59.2 -> 7.48 mm, vias 2 -> 1
- net Net-(C19-Pad2): track 60.1 -> 9.34 mm, vias 1 -> 2
- net USB_5: track 0.00 -> 49.4 mm
- net Net-(C21-Pad2): track 42.1 -> 6.66 mm, vias 1 -> 0
- net +3v3: track 0.00 -> 35.0 mm, vias 0 -> 4
- net +3.3V: track 31.7 -> 0.00 mm, vias 2 -> 0
- net Net-(C37-Pad1): track 29.5 -> 0.00 mm
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- added copper zone on In2.Cu, net +5V
- added copper zone on In1.Cu, net GND
- removed copper zone on B.Cu, net GND
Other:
- board size 73.2 x 66.8 mm -> 95.2 x 67.5 mm
- copper layers 2 -> 4
- board text added: "+4.1V"
- board text added: "+5V"
- board text added: "6 port USB Power meter v2.2"
- board text added: "Aleks IC"
- board text added: "GND"
- board text added: "MI"
- board text added: "MO"
- board text added: "RST"
- board text added: "RX"
- board text added: "SCK"
- board text added: "SCL"
- board text added: "SDA"
- board text added: "SS"
- board text added: "TX"
- board text removed: "6 port USB Power meter v2.1"
